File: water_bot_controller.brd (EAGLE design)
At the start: 100 x 80 mm, 103 parts, among them IC1 ULN2803A, U2 LM3480IM3-5.0

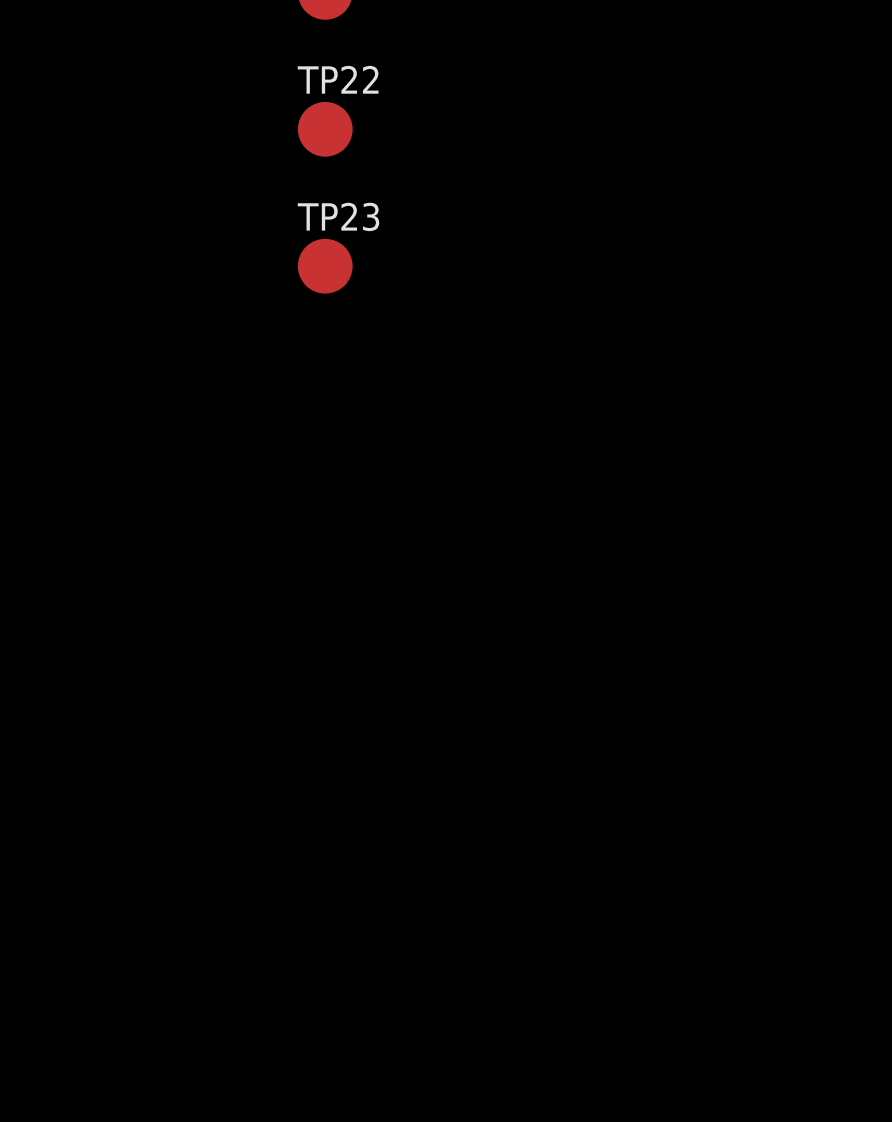
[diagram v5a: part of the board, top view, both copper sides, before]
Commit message: added 12v power conditioning
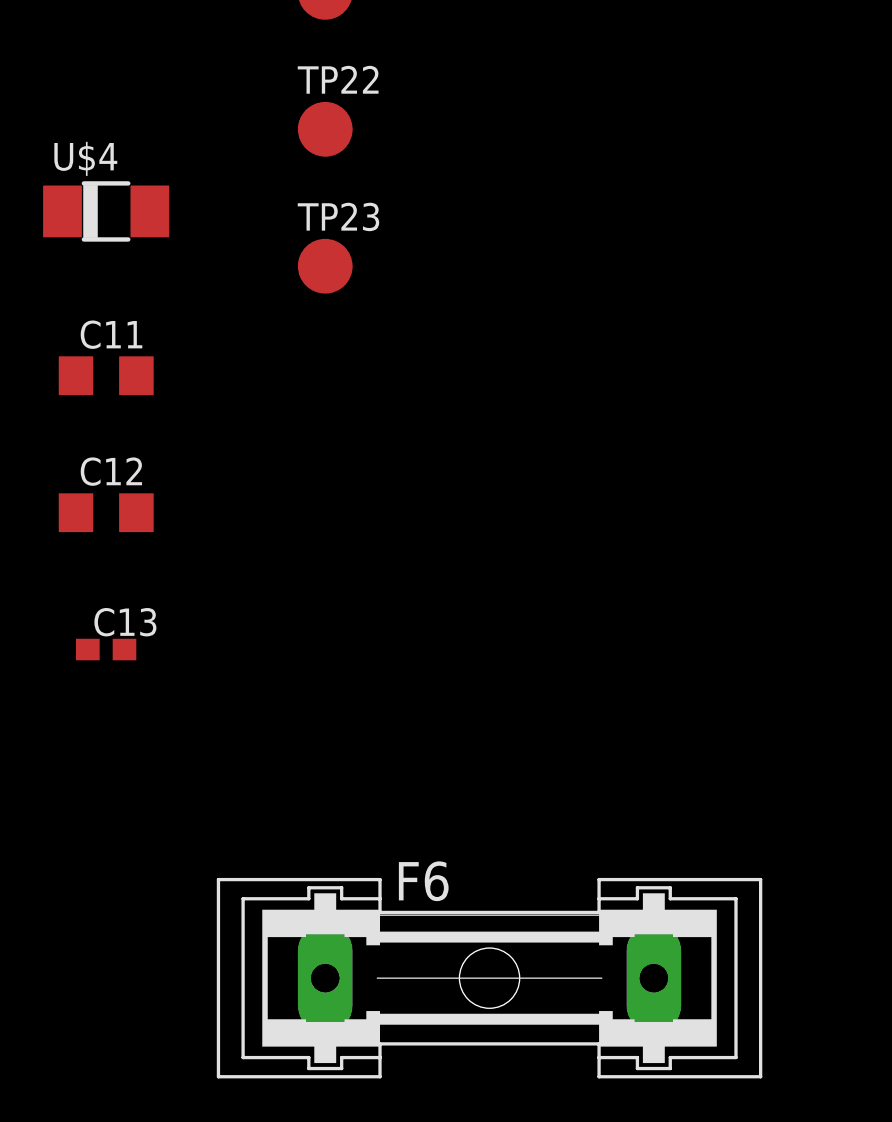
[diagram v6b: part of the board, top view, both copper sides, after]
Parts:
- added C11: 10uF, rcl:C1206
- added C12: 4.7uF, rcl:C1206
- added C13: 0.1uF, rcl:C0603
- added F6: (no value), fuse:GSH15
- added U$4: SMAJ14A, openag_diodes:DO-214AC
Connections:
- net +12V: now also F6.2
- net 12V_IN: now also C11.1, C12.1, C13.1, F6.1, U$4.C
- net GND1: now also C11.2, C12.2, C13.2, U$4.A
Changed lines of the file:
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@@
 <attribute name="TP_SIGNAL_NAME" value="" x="-184.15" y="-1144.27" size="1.778" layer="27" display="off"/>
+</element>
+<element name="U$4" library="openag_diodes" package="DO-214AC" value="SMAJ14A" x="-194.31" y="-1141.73"/>
+<element name="C11" library="rcl" library_urn="urn:adsk.eagle:library:334" package="C1206" package3d_urn="urn:adsk.eagle:package:23618/2" value="10uF" x="-194.31" y="-1149.35"/>
+<element name="C12" library="rcl" library_urn="urn:adsk.eagle:library:334" package="C1206" package3d_urn="urn:adsk.eagle:package:23618/2" value="4.7uF" x="-194.31" y="-1155.7"/>
+<element name="C13" library="rcl" library_urn="urn:adsk.eagle:library:334" package="C0603" package3d_urn="urn:adsk.eagle:package:23616/2" value="0.1uF" x="-194.31" y="-1162.05"/>
+<element name="F6" library="fuse" library_urn="urn:adsk.eagle:library:233" package="GSH15" package3d_urn="urn:adsk.eagle:package:14065/1" value="" x="-176.53" y="-1177.29">
+<attribute name="MF" value="" x="-176.53" y="-1177.29" size="1.778" layer="27" display="off"/>
+<attribute name="MPN" value="64900001039" x="-176.53" y="-1177.29" size="1.778" layer="27" display="off"/>
+<attribute name="OC_FARNELL" value="1271673" x="-176.53" y="-1177.29" size="1.778" layer="27" display="off"/>
+<attribute name="OC_NEWARK" value="02P0318" x="-176.53" y="-1177.29" size="1.778" layer="27" display="off"/>
 </element>
 </elements>
@@
 <contactref element="RELAY_5" pad="1"/>
 <contactref element="R24" pad="1"/>
+<contactref element="F6" pad="2"/>
 <wire x1="-73.66" y1="-678.5356" x2="-79.6544" y2="-680.5422" width="0" layer="19" extent="1-1"/>
 <wire x1="-79.6544" y1="-610.6922" x2="-73.66" y2="-678.5356" width="0" layer="19" extent="1-1"/>
@@
 <wire x1="-23.7744" y1="24.3078" x2="-12.7" y2="-50.8" width="0" layer="19" extent="1-1"/>
 <wire x1="-17.78" y1="26.3144" x2="-23.7744" y2="24.3078" width="0" layer="19" extent="1-1"/>
+<wire x1="-168.91" y1="-1177.29" x2="-79.6544" y2="-680.5422" width="0" layer="19" extent="1-1"/>
 </signal>
 <signal name="N$2">
@@
 <contactref element="TP18" pad="TP"/>
 <contactref element="TP20" pad="TP"/>
+<contactref element="U$4" pad="A"/>
+<contactref element="C11" pad="2"/>
+<contactref element="C12" pad="2"/>
+<contactref element="C13" pad="2"/>
 <wire x1="-181.61" y1="-1067.32" x2="-186.69" y2="-1067.32" width="0" layer="19" extent="1-1"/>
 <wire x1="-176.53" y1="-1067.32" x2="-181.61" y2="-1067.32" width="0" layer="19" extent="1-1"/>
@@
 <wire x1="-184.15" y1="-1112.52" x2="-184.15" y2="-1106.17" width="0" layer="19" extent="1-1"/>
 <wire x1="-184.15" y1="-1125.22" x2="-184.15" y2="-1112.52" width="0" layer="19" extent="1-1"/>
+<wire x1="-192.285" y1="-1141.73" x2="-184.15" y2="-1125.22" width="0" layer="19" extent="1-1"/>
+<wire x1="-192.91" y1="-1149.35" x2="-192.285" y2="-1141.73" width="0" layer="19" extent="1-1"/>
+<wire x1="-192.91" y1="-1155.7" x2="-192.91" y2="-1149.35" width="0" layer="19" extent="1-1"/>
+<wire x1="-193.46" y1="-1162.05" x2="-192.91" y2="-1155.7" width="0" layer="19" extent="1-1"/>
 <wire x1="-111.76" y1="-937.26" x2="-131.445" y2="-1026.22" width="0" layer="19" extent="1-1"/>
 <wire x1="-78.74" y1="-144.28" x2="-111.76" y2="-937.26" width="0" layer="19" extent="1-1"/>
@@
 <contactref element="+12V" pad="1"/>
 <contactref element="TP21" pad="TP"/>
+<contactref element="C11" pad="1"/>
+<contactref element="C12" pad="1"/>
+<contactref element="C13" pad="1"/>
+<contactref element="F6" pad="1"/>
+<contactref element="U$4" pad="C"/>
+<wire x1="-195.16" y1="-1162.05" x2="-184.15" y2="-1177.29" width="0" layer="19" extent="1-1"/>
+<wire x1="-195.71" y1="-1155.7" x2="-195.16" y2="-1162.05" width="0" layer="19" extent="1-1"/>
+<wire x1="-195.71" y1="-1149.35" x2="-195.71" y2="-1155.7" width="0" layer="19" extent="1-1"/>
+<wire x1="-196.335" y1="-1141.73" x2="-195.71" y2="-1149.35" width="0" layer="19" extent="1-1"/>
+<wire x1="-184.15" y1="-1131.57" x2="-196.335" y2="-1141.73" width="0" layer="19" extent="1-1"/>
 <wire x1="-111.76" y1="-905.51" x2="-184.15" y2="-1131.57" width="0" layer="19" extent="1-1"/>
 </signal>
